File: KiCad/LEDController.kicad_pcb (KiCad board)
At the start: 4 copper layers, 50 x 50 mm, 40 parts, among them J1 Conn_01x05, J2 UART, J3 JTAG, J5 USB_C_Receptacle_USB2.0_16P, J6 Conn_01x03, J7 VDD, J8 GND, J9 Conn_01x14, Q1 IRLZ44N, Q2 IRLZ44N, Q3 IRLZ44N, Q4 IRLZ44N, SW1 BOOT, SW2 ENABLE, U1 TPS62132, U2 ESP32-S3-WROOM-2

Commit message: .
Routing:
- net +24V: track 76.7 -> 88.9 mm
- net GND: track 12.8 -> 2.60 mm
- net ESP_BOOT: track 0.00 -> 4.31 mm
- net ESP_EN: track 7.02 -> 9.04 mm
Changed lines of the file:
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@@
+	)
+	(segment
+		(start 124.75 77.75)
+		(end 123.7085 76.7085)
+		(width 1)
+		(locked yes)
+		(layer "F.Cu")
+		(net 1)
 	)
 	(segment
@@
 	)
 	(segment
+		(start 123.7085 76.7085)
+		(end 123.7085 73.483)
+		(width 1)
+		(locked yes)
+		(layer "F.Cu")
+		(net 1)
+	)
+	(segment
 		(start 112.535 94.4065)
 		(end 110.1915 96.75)
@@
 	)
 	(segment
+		(start 121.2303 73.4063)
+		(end 121.2303 73.406)
+		(width 1)
+		(locked yes)
+		(layer "F.Cu")
+		(net 1)
+	)
+	(segment
 		(start 110.1915 96.75)
 		(end 94 96.75)
@@
 	)
 	(segment
-		(start 124.75 92.3515)
-		(end 124.75 86)
-		(width 1)
-		(locked yes)
-		(layer "F.Cu")
-		(net 1)
-	)
-	(segment
 		(start 121.2303 73.406)
 		(end 121.2303 72.2669)
@@
 	)
 	(segment
+		(start 124.75 92.3515)
+		(end 124.75 77.75)
+		(width 1)
+		(locked yes)
+		(layer "F.Cu")
+		(net 1)
+	)
+	(segment
 		(start 121.2303 72.8367)
 		(end 121.2303 73.406)
@@
 	)
 	(segment
-		(start 123.4043 73.4482)
-		(end 123.9556 73.9995)
-		(width 1)
-		(locked yes)
-		(layer "F.Cu")
-		(net 1)
-	)
-	(segment
-		(start 97.295 94.4065)
-		(end 107.455 94.4065)
-		(width 1)
-		(layer "F.Cu")
-		(net 2)
+		(start 121.2685 73.4445)
+		(end 121.2303 73.4063)
+		(width 1)
+		(locked yes)
+		(layer "F.Cu")
+		(net 1)
 	)
 	(segment
@@
 	)
 	(segment
+		(start 123 56)
+		(end 123 57.5725)
+		(width 0.3)
+		(locked yes)
+		(layer "F.Cu")
+		(net 5)
+	)
+	(segment
 		(start 96.531 59.551)
 		(end 96.684 59.398)
@@
 		(layer "F.Cu")
 		(net 5)
+	)
+	(segment
+		(start 123 57.5725)
+		(end 122.682 57.8905)
+		(width 0.3)
+		(locked yes)
+		(layer "F.Cu")
+		(net 5)
+	)
+	(segment
+		(start 120.65 56.4)
+		(end 120.65 57.8905)
+		(width 0.3)
+		(locked yes)
+		(layer "F.Cu")
+		(net 6)
+	)
+	(segment
+		(start 118 56)
+		(end 120.25 56)
+		(width 0.3)
+		(locked yes)
+		(layer "F.Cu")
+		(net 6)
+	)
+	(segment
+		(start 120.25 56)
+		(end 120.65 56.4)
+		(width 0.3)
+		(locked yes)
+		(layer "F.Cu")
+		(net 6)
 	)
 	(segment
@@
 		)
 	)
-	(group ""
-		(locked yes)
-		(members "01828b56-34e0-4a06-a3bf-28ad11a34c5a" "1c7e8a6f-f2f5-4e6d-a802-88a13df24168"
-			"21bdb9d8-bf2f-453b-bcd4-2856f7a4a413" "457147a2-ef18-45b0-b280-cf6765241b55"
-			"46141387-b783-4eca-88e7-9b1fef433324" "5a9325b2-5d57-4d75-b5a9-3242ae65519b"
-			"692bf279-3e98-42e2-8c72-cc135f14818b" "84f42245-9690-4e30-ae27-08fc111fd4a3"
-			"92405c58-db03-4148-bb69-0bfeaf815f0a" "94ee00f1-81c6-40c2-9a85-2dcfd6776d02"
-			"a7e7a91f-8641-4af0-b3ef-a454fbc7569a" "a94018c4-9228-4e0f-9750-be65928fefcd"
-			"aa58f986-5f5b-482f-8677-e671ee6c0a88" "ae2c4346-d1d5-498d-81ad-7d7f909279ac"
-			"b9324584-4b93-42a0-baa1-b42d30034026" "c2ba79c6-28e2-4018-99fe-8b7b30e6304f"
-			"c2ca5805-b247-466d-9a6d-d8db4c54b930" "c3204412-d963-4cae-af26-e04c5b9c5683"
-			"c5f66cfd-3a2a-411a-af6f-0376a95c4a74" "d210df41-780c-4e85-82f6-d132ecebb21c"
-			"d22ce7e1-464b-41e7-a746-925fdb4bc739" "d59aea36-8e0b-4e55-a1ef-fd7072b163ae"
-			"dc29fb80-82c3-42fd-8468-10d0b983914a" "dffcf38c-12da-4939-994c-b450ebcf85a3"
-			"e88183c6-135c-484d-aca6-c18ac4f7a445" "ecdc397c-6dbc-4ad7-9db0-883d03c6996f"
-			"efce23ec-90b2-498e-bf46-94fa4c1abbe8" "f69433e8-45e1-4a71-8aa0-e3f665ab8def"
-			"f856bc97-eb50-4a21-896d-e43ce4389c5f" "ffae4f2f-3083-49c5-b2c9-3705d5b3ecf3"
-		)
-	)

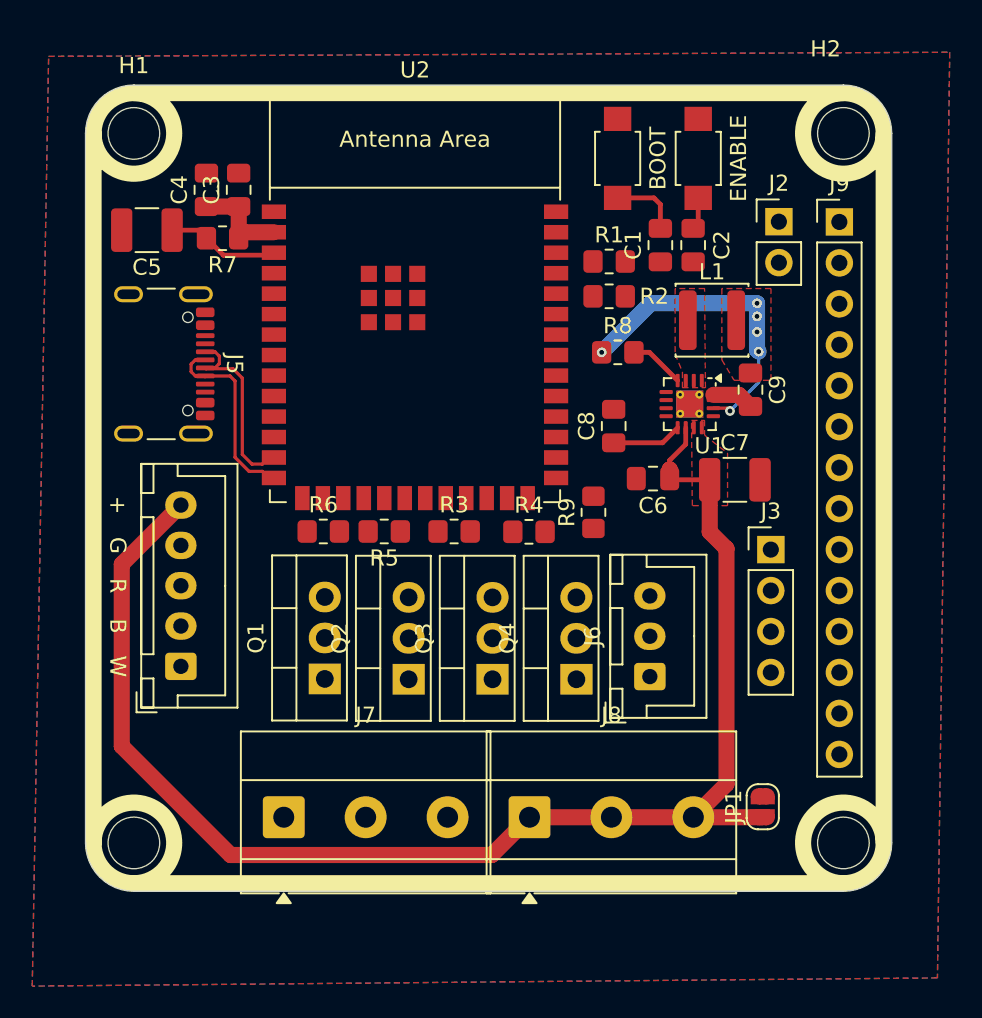
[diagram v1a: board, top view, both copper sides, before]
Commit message: add different buck converter
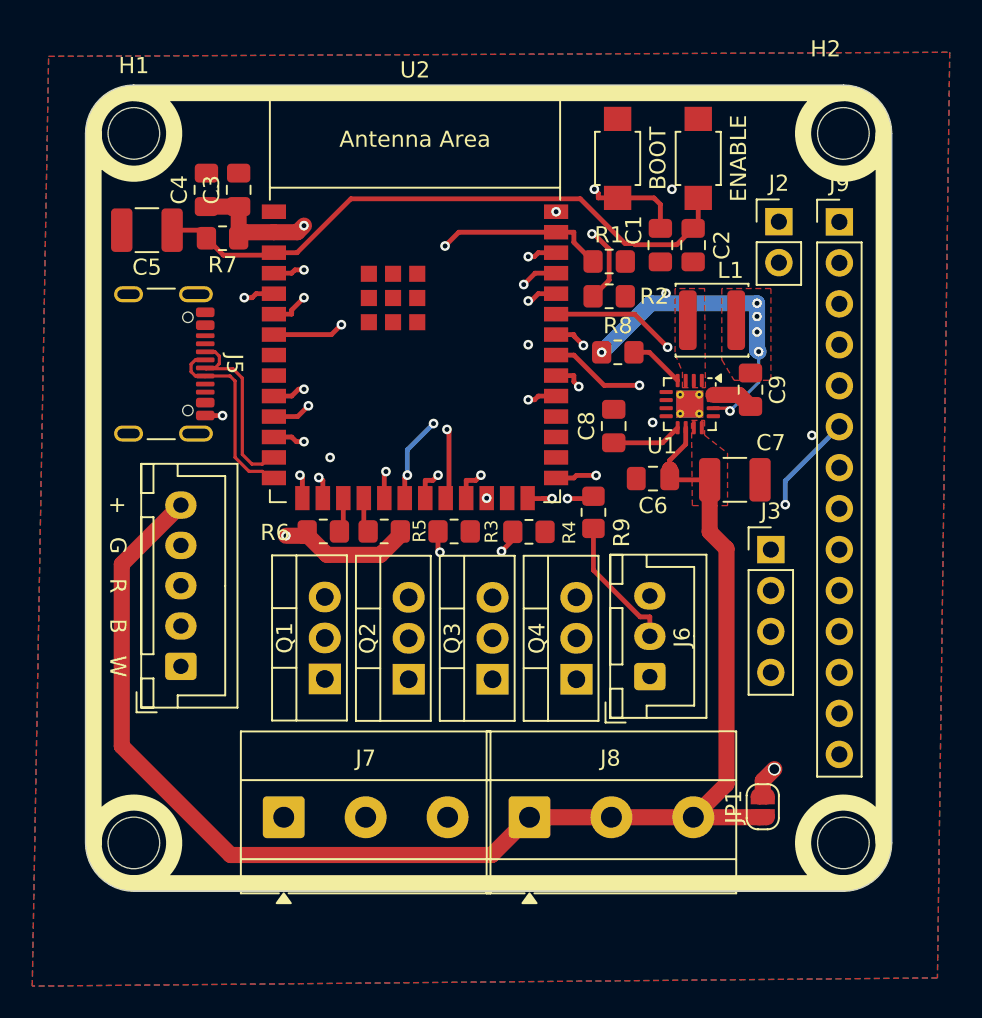
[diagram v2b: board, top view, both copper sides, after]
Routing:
- net +3.3V: track 25.8 -> 89.4 mm, vias 6 -> 10
- net GPIO.6: track 0.00 -> 47.3 mm, vias 0 -> 1
- net GPIO.11: track 0.00 -> 45.4 mm, vias 0 -> 1
- net GPIO.8: track 0.00 -> 42.9 mm, vias 0 -> 1
- net GPIO.18: track 0.00 -> 40.0 mm, vias 0 -> 1
- net GPIO.46: track 0.00 -> 39.8 mm, vias 0 -> 1
- net GPIO.17: track 0.00 -> 39.0 mm, vias 0 -> 1
- net G: track 0.00 -> 38.6 mm, vias 0 -> 2
- net R: track 0.00 -> 38.0 mm, vias 0 -> 1
- net GPIO.7: track 0.00 -> 36.9 mm, vias 0 -> 1
- net W: track 0.00 -> 36.1 mm, vias 0 -> 3
- net GPIO.38: track 0.00 -> 35.5 mm, vias 0 -> 2
- net GPIO.12: track 0.00 -> 33.8 mm, vias 0 -> 2
- net Data: track 0.00 -> 33.0 mm, vias 0 -> 3
- net GPIO.47: track 0.00 -> 32.6 mm, vias 0 -> 1
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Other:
- board text added: "+5-24V"
- board text added: "GND"

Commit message: rearrange again, route
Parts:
- removed C6: 100n, Capacitor_SMD:C_0805_2012Metric_Pad1.18x1.45mm_HandSolder
- removed C7: 10u, Capacitor_SMD:C_1210_3225Metric_Pad1.33x2.70mm_HandSolder
- removed C8: 3.3n, Capacitor_SMD:C_0805_2012Metric_Pad1.18x1.45mm_HandSolder
- removed C9: 22u, Capacitor_SMD:C_0805_2012Metric_Pad1.18x1.45mm_HandSolder
- removed L1: 1/2.2u, Inductor_SMD:L_APV_ANR4026
- removed R8: 100k, Resistor_SMD:R_0805_2012Metric_Pad1.20x1.40mm_HandSolder
- removed U1: TPS62132, Package_DFN_QFN:VQFN-16-1EP_3x3mm_P0.5mm_EP1.68x1.68mm_ThermalVias
- added C10: 100n, Capacitor_SMD:C_0805_2012Metric_Pad1.18x1.45mm_HandSolder, F.Cu at (102.6, 61.2)
- added C11: 100n, Capacitor_SMD:C_0805_2012Metric_Pad1.18x1.45mm_HandSolder, F.Cu at (102.5, 70.3)
- added C12: 10u, Capacitor_SMD:C_1210_3225Metric_Pad1.33x2.70mm_HandSolder, F.Cu at (103.0, 67.5)
- added C15: 10u, Capacitor_SMD:C_1210_3225Metric_Pad1.33x2.70mm_HandSolder, F.Cu at (97.8, 68.1)
- added L2: 15u, Inductor_SMD:L_APV_ANR4026, F.Cu at (97.8, 64.0)
- added R12: 100k, Resistor_SMD:R_0805_2012Metric_Pad1.20x1.40mm_HandSolder, F.Cu at (105.7, 64.0)
- added R13: 1.8k, Resistor_SMD:R_0805_2012Metric_Pad1.20x1.40mm_HandSolder, F.Cu at (106.6, 67.8)
- added R14: 20k, Resistor_SMD:R_0805_2012Metric_Pad1.20x1.40mm_HandSolder, F.Cu at (106.3, 70.5)
- added U3: TPS54202DDC, Package_TO_SOT_SMD:SOT-23-6, F.Cu at (102.6, 64.0)
- R1, R2, R3, R4, R5, R6: moved to B.Cu
- moved C1 31.1 mm to (89.7, 56.6), turned to 0 degrees
- moved R1 25.4 mm to (97.8, 75.9), turned to 90 degrees
- moved SW1 24.8 mm to (93.2, 53.3)
- moved SW2 24.7 mm to (98.3, 53.3)
- moved J2 22.1 mm to (106.7, 51.8), turned to -90 degrees
- moved C2 20.8 mm to (102.4, 54.6), turned to 180 degrees
- moved R2 20.5 mm to (102.4, 75.9), turned to 90 degrees
- moved R6 15.1 mm to (113.8, 71.1), turned to -90 degrees
- moved R9 14.5 mm to (107.7, 64.0)
- moved R7 13.8 mm to (107.2, 60.2)
- moved C3 13.7 mm to (108.2, 56.1)
- moved C4 13.7 mm to (106.2, 56.1)
- moved C5 13.6 mm to (102.4, 57.7)
- moved U2 13.6 mm to (119.0, 65.0)
- moved R5 13.5 mm to (115.8, 71.1), turned to -90 degrees
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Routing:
- net GPIO.6: track 47.3 -> 0.00 mm, vias 1 -> 0
- net +3.3V: track 89.4 -> 43.9 mm, vias 10 -> 3
- net GPIO.11: track 45.4 -> 0.00 mm, vias 1 -> 0
- net GPIO.8: track 42.9 -> 0.00 mm, vias 1 -> 0
- net GPIO.18: track 40.0 -> 0.00 mm, vias 1 -> 0
- net GPIO.46: track 39.8 -> 0.00 mm, vias 1 -> 0
- net GPIO.17: track 39.0 -> 0.00 mm, vias 1 -> 0
- net GPIO.7: track 36.9 -> 0.00 mm, vias 1 -> 0
- net GPIO.38: track 35.5 -> 0.00 mm, vias 2 -> 0
- net GPIO.12: track 33.8 -> 0.00 mm, vias 2 -> 0
- net GPIO.47: track 32.6 -> 0.00 mm, vias 1 -> 0
- net JTAG.MTMS: track 31.9 -> 0.00 mm, vias 1 -> 0
- net GPIO.13: track 31.1 -> 0.00 mm, vias 2 -> 0
- net GPIO.45: track 30.2 -> 0.00 mm, vias 1 -> 0
- net GPIO.14: track 30.1 -> 0.00 mm, vias 1 -> 0
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- added copper zone on F.Cu, net Net-(U3-SW)
- removed copper zone on F.Cu, net +24V
- removed copper zone on F.Cu, net +3.3V
- removed copper zone on F.Cu, net /3.3V Switch

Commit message: .
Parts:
- added C14: 10u, Capacitor_SMD:C_1210_3225Metric_Pad1.33x2.70mm_HandSolder, F.Cu at (97.8, 71.4)
- SW2: value ENABLE -> EN
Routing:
- net GPIO.17: track 0.00 -> 35.5 mm, vias 0 -> 2
- net JTAG.MTMS: track 0.00 -> 29.6 mm, vias 0 -> 1
- net GPIO.7: track 0.00 -> 28.5 mm, vias 0 -> 1
- net UART.RX: track 0.00 -> 27.7 mm, vias 0 -> 1
- net GPIO.18: track 0.00 -> 27.4 mm, vias 0 -> 1
- net GPIO.8: track 0.00 -> 27.4 mm, vias 0 -> 1
- net UART.TX: track 0.00 -> 25.3 mm, vias 0 -> 1
- net GPIO.46: track 0.00 -> 24.7 mm
- net GPIO.6: track 0.00 -> 23.8 mm, vias 0 -> 1
- net GPIO.47: track 0.00 -> 23.5 mm, vias 0 -> 1
- net JTAG.MTDI: track 0.00 -> 21.6 mm, vias 0 -> 1
- net GPIO.11: track 0.00 -> 20.0 mm, vias 0 -> 1
- net GPIO.12: track 0.00 -> 17.2 mm, vias 0 -> 1
- net GPIO.38: track 0.00 -> 17.1 mm, vias 0 -> 1
- net JTAG.MTDO: track 0.00 -> 17.0 mm, vias 0 -> 1
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
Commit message: .
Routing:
- net unconnected-(J5-SHIELD-PadS1)_3: track 0.00 -> 19.5 mm
- net GPIO.17: track 35.5 -> 25.0 mm, vias 2 -> 1
- net GPIO.7: track 28.5 -> 23.3 mm
- net GPIO.11: track 20.0 -> 22.9 mm
- net GPIO.18: track 27.4 -> 25.0 mm
- net GPIO.47: track 23.5 -> 25.8 mm
- net +24V: track 82.3 -> 80.3 mm
- net GPIO.14: track 15.6 -> 13.8 mm
- net JTAG.MTCK: track 12.7 -> 11.0 mm
- net GPIO.38: track 17.1 -> 18.1 mm
- net GPIO.45: track 16.0 -> 16.9 mm

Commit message: add led
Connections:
- J9 pad 1: GPIO.6 -> +3.3V
- J9 pad 2: GPIO.7 -> GND
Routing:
- net GPIO.6: track 23.8 -> 0.00 mm, vias 1 -> 0
- net GPIO.7: track 23.3 -> 0.00 mm, vias 1 -> 0
- net +3.3V: track 54.0 -> 75.7 mm
- net GPIO.46: track 24.7 -> 26.8 mm
- net GND: vias 9 -> 23

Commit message: .
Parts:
- added C6: 10u, Capacitor_SMD:C_0805_2012Metric_Pad1.18x1.45mm_HandSolder, F.Cu at (97.8, 71.4)
- added D1: LED, LED_SMD:LED_0603_1608Metric_Pad1.05x0.95mm_HandSolder, F.Cu at (103.5, 74.3)
- added R8: 100, Resistor_SMD:R_0805_2012Metric_Pad1.20x1.40mm_HandSolder, F.Cu at (107.1, 74.3)
- C12, C14, C15, C5: footprint Capacitor_SMD:C_1210_3225Metric_Pad1.33x2.70mm_HandSolder -> Capacitor_SMD:C_0805_2012Metric_Pad1.18x1.45mm_HandSolder
- moved C14 2.03 mm to (97.8, 69.3)
- moved C5 0.80 mm to (102.6, 58.4)
- moved C15 0.76 mm to (97.8, 67.3)
- moved R7 0.51 mm to (106.7, 60.2)
- moved C12 0.42 mm to (102.6, 67.6)
- moved R14 0.36 mm to (106.7, 70.6)
- moved C11 0.34 mm to (102.6, 70.6)
- moved R13 0.10 mm to (106.7, 67.8)
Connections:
- U2 pad 7: GPIO.7 -> unconnected-(U2-GPIO7/TOUCH7/ADC1_CH6-Pad7)
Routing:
- net GPIO.6: track 0.00 -> 16.3 mm, vias 0 -> 2
- net Net-(D1-A): track 0.00 -> 1.68 mm
- net ESP_EN: track 16.3 -> 17.2 mm
- net Net-(R13-Pad2): track 2.63 -> 3.28 mm
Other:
- board text added: "VDD"

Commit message: .
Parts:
- moved J7 1.19 mm to (130.6, 57.5)
- renumbered C14 to C10, C15 to C11, C10 to C6, C11 to C7, C12 to C8, C6 to C9, J2 to J1, J7 to J2, J8 to J3, J1 to J4, J6 to J5, J5 to J6, J9 to J7, J3 to J8, L2 to L1, R12 to R10, R13 to R11, R14 to R12, R9 to R7, R7 to R9, U3 to U1
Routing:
- net unconnected-(J6-SHIELD-PadS1)_3: track 19.5 -> 0.00 mm
- net GPIO.38: track 18.1 -> 24.7 mm, vias 1 -> 2
- net GND: track 6.82 -> 2.31 mm, vias 23 -> 21
- net GPIO.47: track 25.8 -> 28.7 mm
- net GPIO.45: track 16.9 -> 19.0 mm
- net GPIO.12: track 17.2 -> 19.0 mm
- net GPIO.13: track 14.9 -> 16.3 mm
- net G: track 51.0 -> 49.8 mm
- net JTAG.MTDI: track 21.7 -> 20.7 mm
- net GPIO.8: track 27.4 -> 28.4 mm
- net GPIO.46: track 26.8 -> 27.7 mm
- net GPIO.21: track 13.0 -> 14.0 mm
- net GPIO.17: track 25.0 -> 26.0 mm
- net GPIO.11: track 22.9 -> 23.9 mm
- net +3.3V: track 75.3 -> 76.2 mm
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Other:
- board text added: "LED Controller Designed by ${COMPANY} ${CURRENT_DATE} V${REVISION}"
- board text added: "PH"
- board text added: "RX"
- board text added: "TX"
